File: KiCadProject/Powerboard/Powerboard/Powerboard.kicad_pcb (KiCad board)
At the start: 2 copper layers, 45 x 45 mm, 25 parts, among them J1 XT60, J2 XT30, J3 Conn_01x03_Male, Q1 SIR696DP-T1-GE3, Q2 SUD50P10-43L-GE3, U1 MAX16833

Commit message: Much more refinement. Re-selected some components for more logical ones. Got all 3d models in place.
Signed-off-by: Eldalote.Electronics <Eldalote.Electronics@gmail.com>
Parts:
- added C1: Connector cap, Capacitor_SMD:CP_Elec_5x5.3, F.Cu at (133.0, 94.0)
- added C3: 100n, Capacitor_SMD:C_0402_1005Metric, F.Cu at (149.0, 102.0)
- added NT1: NetTie_2, NetTie:NetTie-2_SMD_Pad0.5mm, F.Cu at (153.5, 104.5)
- C4: renamed from C2; footprint Capacitor_SMD:C_0603_1608Metric -> Capacitor_SMD:C_0402_1005Metric
- C5: renamed from C3; value 220n/390n -> 220n; footprint Capacitor_SMD:C_0805_2012Metric -> Capacitor_SMD:C_0603_1608Metric
- L1: value SRP1265C-6R8M -> 6u8
- Q1: value SIR696DP-T1-GE3 -> Q_NMOS_GDS; footprint Ultralibrarianfootprints:SIR696DP-T1-GE3 -> Package_TO_SOT_SMD:TO-252-2
- R1: renamed from R3; footprint Resistor_SMD:R_0603_1608Metric -> Resistor_SMD:R_0402_1005Metric
- R10: value 330m/130m -> 330m
- R2: renamed from R1; footprint Resistor_SMD:R_0603_1608Metric -> Resistor_SMD:R_0402_1005Metric
- R3: renamed from R2; footprint Resistor_SMD:R_0603_1608Metric -> Resistor_SMD:R_0402_1005Metric
- R4: value 953R/120R -> 953R
- R5: value 4k7/2k7 -> 4k7; footprint Resistor_SMD:R_0603_1608Metric -> Resistor_SMD:R_0402_1005Metric
- R6: value 51m/33m -> 51m; footprint Resistor_SMD:R_0603_1608Metric -> Resistor_SMD:R_1206_3216Metric
- R7: footprint Resistor_SMD:R_0805_2012Metric -> Resistor_SMD:R_0603_1608Metric
- R8: value 5M1/4M75 -> 5M1
- R9: footprint Resistor_SMD:R_0603_1608Metric -> Resistor_SMD:R_0402_1005Metric
- moved J3 55.6 mm to (121.0, 106.5)
- moved R6 12.5 mm to (164.0, 114.0)
- moved Q2 9.69 mm to (156.0, 114.5)
- moved Q1 9.49 mm to (163.9, 105.2)
- moved R7 8.86 mm to (150.0, 108.0)
- moved C4 8.78 mm to (149.0, 104.0)
- moved R5 8.66 mm to (149.0, 106.0)
- moved C2 8.63 mm to (145.0, 101.9)
- moved J2 8.62 mm to (146.0, 117.0)
- moved R3 8.60 mm to (139.0, 103.5)
- moved C9 8.50 mm to (156.0, 95.5), turned to 90 degrees
- moved L1 8.42 mm to (153.0, 86.0)
- moved U1 8.35 mm to (144.0, 106.1)
- moved C5 8.08 mm to (137.7, 109.2)
- moved R4 8.08 mm to (137.9, 111.3)
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- renumbered C1 to C2, C4 to C6, C5 to C7, C6 to C8, C7 to C9
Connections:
- net /ISENSE-R renamed /Vout-FET
- C6 pad 1: /ISENSE+ -> /V-out
- C7 pad 1: /ISENSE+ -> /V-out
- C8 pad 1: /ISENSE+ -> /V-out
- C9 pad 1: /ISENSE+ -> /V-out
- D1 pad 1: /ISENSE+ -> /V-out
- D1 pad 2: Net-(D1-Pad2) -> /L-out
- L1 pad 2: Net-(D1-Pad2) -> /L-out
- Q1 pad 1: /RCS -> /NDRV
- Q1 pad 2: /RCS -> /L-out
- R10 pad 2: /ISENSE+ -> /V-out
- R8 pad 2: /ISENSE+ -> /V-out
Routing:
- net /ISENSE+: track 0.00 -> 8.08 mm
- net /V-out: track 0.00 -> 3.43 mm
- added copper zone on F.Cu, net /V-out
- added copper zone on B.Cu, net GND
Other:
- copper layers 2 -> 4
- rule pad_to_mask_clearance: 0 -> 0.05
- board text added: "POWER IN"

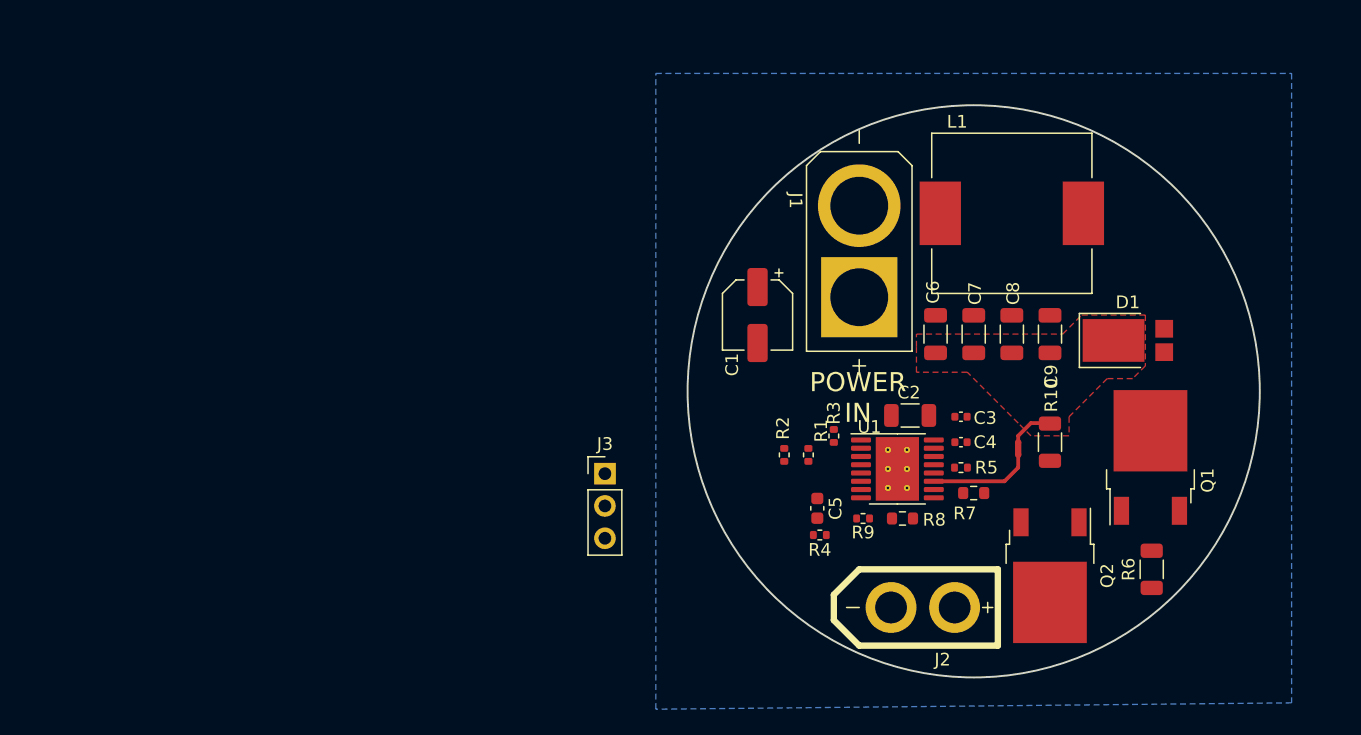
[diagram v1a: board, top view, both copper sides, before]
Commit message: Should be final placement on powerboard now, just finishing touches left.
Signed-off-by: Eldalote.Electronics <Eldalote.Electronics@gmail.com>
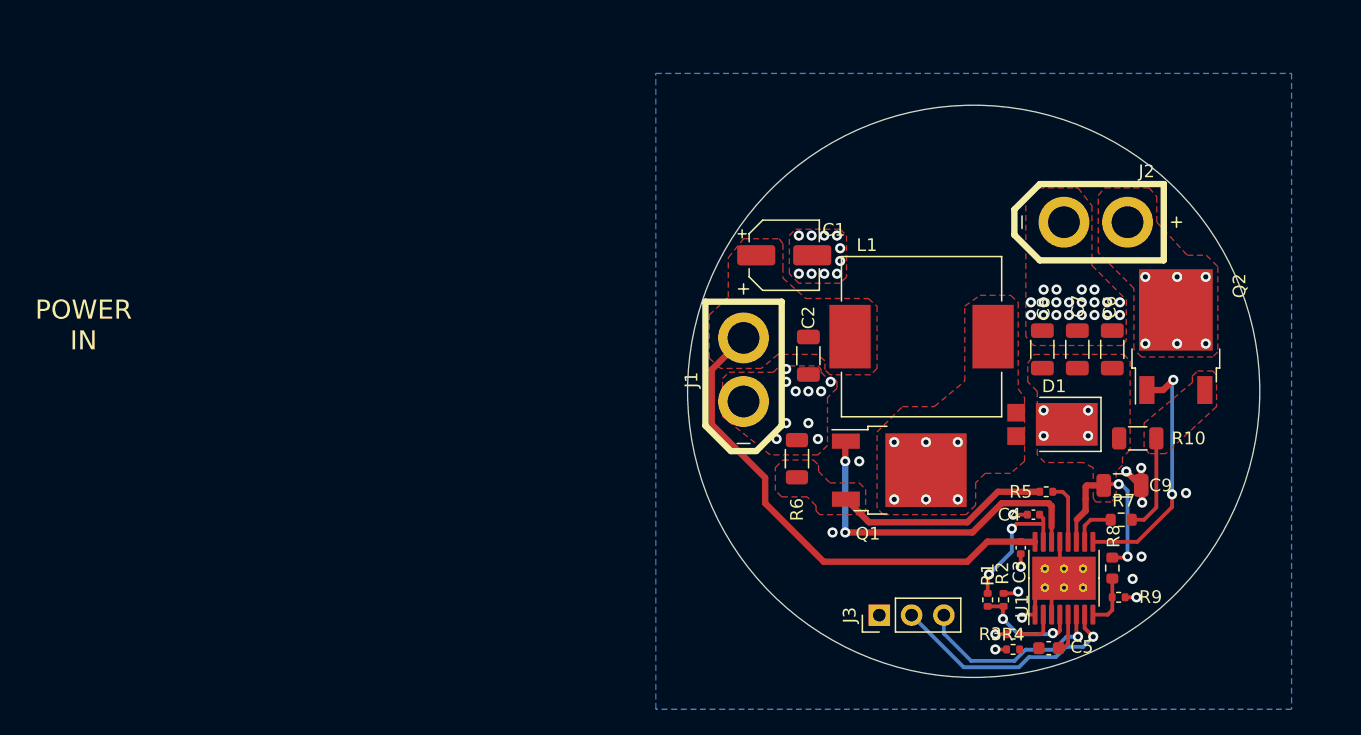
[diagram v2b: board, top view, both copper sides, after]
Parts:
- J1: value XT60 -> XT30; footprint Eldalote-footprints:XT60 -> Eldalote-footprints:XT30
- moved J2 33.2 mm to (159.6, 86.7)
- moved R6 29.2 mm to (136.1, 105.3), turned to -90 degrees
- moved J3 24.3 mm to (142.6, 117.6), turned to 90 degrees
- moved C5 21.3 mm to (155.9, 120.2), turned to 180 degrees
- moved Q2 21.2 mm to (165.9, 95.7), turned to 90 degrees
- moved R9 21.0 mm to (161.4, 116.2), turned to 180 degrees
- moved R3 21.0 mm to (153.1, 119.1), turned to 0 degrees
- moved R2 20.7 mm to (152.3, 116.4)
- moved Q1 19.8 mm to (144.2, 106.2), turned to 0 degrees
- moved R1 18.1 mm to (151.1, 116.4)
- moved R4 17.7 mm to (153.1, 120.3), turned to 0 degrees
- moved R8 17.0 mm to (160.9, 113.9), turned to 90 degrees
- moved U1 15.7 mm to (157.1, 114.7), turned to 90 degrees
- moved C6 14.0 mm to (160.9, 96.7)
- moved C9 13.2 mm to (161.7, 107.4), turned to 0 degrees
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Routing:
- net /IN: track 0.00 -> 39.6 mm
- net /NDRV: track 0.00 -> 27.3 mm, vias 0 -> 2
- net GND: track 0.00 -> 20.2 mm, vias 0 -> 55
- net /!DIMOUT: track 0.00 -> 19.8 mm, vias 0 -> 2
- net /PWMDIM: track 0.00 -> 19.0 mm, vias 0 -> 1
- net /RCS: track 0.00 -> 17.0 mm
- net /!FTL: track 0.00 -> 15.5 mm, vias 0 -> 1
- net /VCC: track 0.00 -> 10.8 mm, vias 0 -> 2
- net /ICTRL: track 0.00 -> 8.61 mm, vias 0 -> 2
- net /Vout-FET: track 0.00 -> 7.77 mm
- net /V-out: track 3.43 -> 10.0 mm, vias 0 -> 6
- net /CS: track 0.00 -> 4.90 mm
- net /ISENSE+: track 8.08 -> 3.64 mm
- net /OPV: track 0.00 -> 4.15 mm
- net /ISENSE-: track 0.00 -> 3.51 mm
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- added copper zone on F.Cu, net /IN
- added copper zone on F.Cu, net /L-out
- added copper zone on F.Cu, net /LED+
- added copper zone on F.Cu, net /RCS
- added copper zone on F.Cu, net /Vout-FET
- added copper zone on F.Cu, net GND
- added copper zone on In1.Cu, net GND
- added copper zone on In2.Cu, net GND
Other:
- board text added: "Input current loop, Kept as small as possible"
- board text added: "Output current loop, Kept as small as possible"

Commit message: Led driver board v0.1 done
Signed-off-by: Eldalote.Electronics <Eldalote.Electronics@gmail.com>
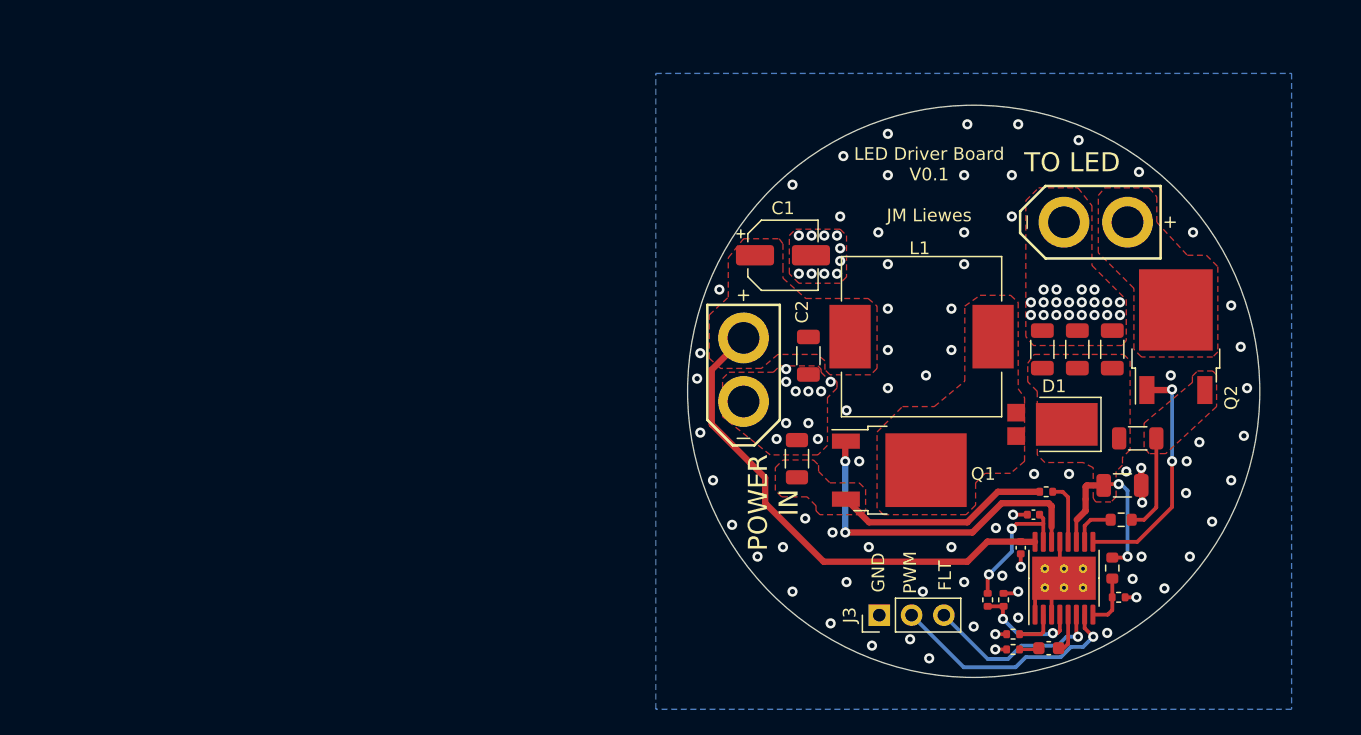
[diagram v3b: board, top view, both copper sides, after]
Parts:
- C1: value Connector cap -> 22u
- J2: footprint Eldalote-footprints:XT30 -> Eldalote-footprints:XT30_Female
- R8: renamed from R4; value 953R -> 910R
- moved C1 0.10 mm to (135.0, 89.3)
- renumbered R3 to R1, R9 to R10, R1 to R2, R2 to R3, R5 to R4, R8 to R5, R10 to R6, R6 to R9
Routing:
- net GND: track 20.2 -> 17.5 mm, vias 55 -> 115
- net /comp_RC: track 0.00 -> 1.56 mm
- net /!DIMOUT: track 19.8 -> 18.6 mm
- net /!FTL: track 15.5 -> 14.5 mm
- net /V-out: vias 6 -> 2
- net /LED+: vias 6 -> 0
- net /L-out: vias 6 -> 0
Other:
- board text added: "FLT"
- board text added: "GND"
- board text added: "LED Driver Board V0.1 JM Liewes"
- board text added: "PWM"
- board text added: "TO LED"
- board text added: "jlcjlcjlcjlc"
